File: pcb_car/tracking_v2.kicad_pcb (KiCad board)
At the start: 2 copper layers, 75 x 64 mm, 24 parts, among them J1 Conn_01x02, J2 Conn_01x02, J3 Conn_01x02, J4 Conn_01x02, J5 Conn_01x16_Female, J6 Conn_01x02, J7 Conn_01x20_Female, J8 Conn_01x03, J9 Conn_01x03, SW1 SW_Push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

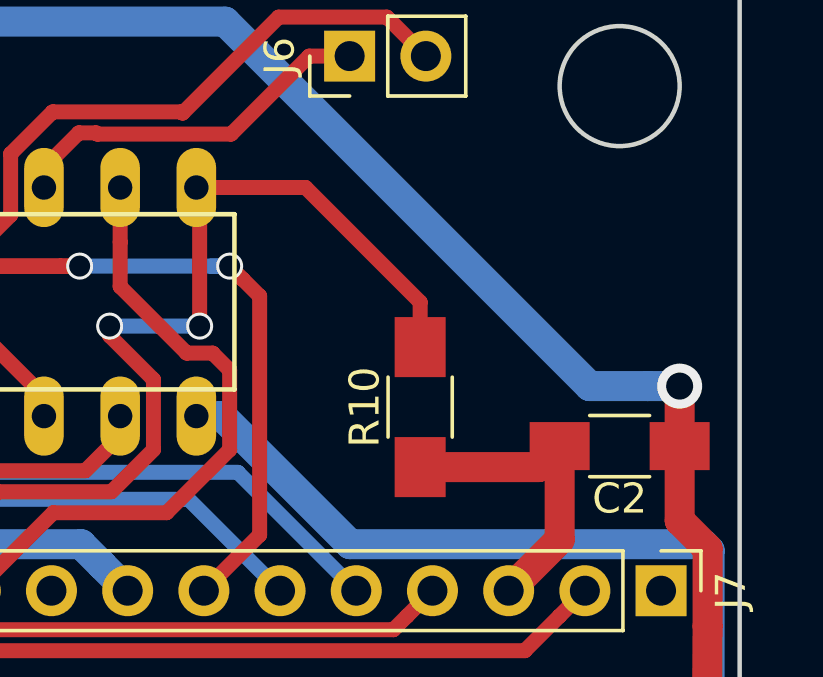
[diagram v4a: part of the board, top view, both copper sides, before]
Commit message: modifications for silkscreen
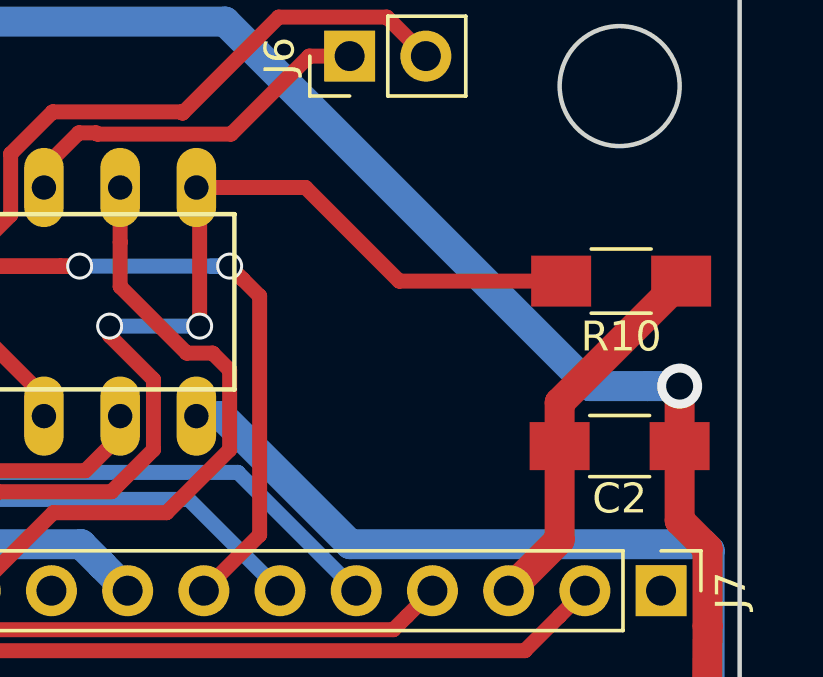
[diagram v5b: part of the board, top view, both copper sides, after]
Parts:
- moved R10 7.91 mm to (190.1, 84.5), turned to 180 degrees
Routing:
- net EN2_B: track 34.0 -> 36.9 mm
- net GND: track 207.0 -> 209.4 mm
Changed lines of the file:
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@@
 (kicad_pcb (version 4) (host pcbnew 4.0.7)
   (general
-    (links 71)
-    (no_connects 3)
-    (area 118.924999 73.924999 194.075001 138.075001)
+    (links 69)
+    (no_connects 0)
+    (area 109.899999 61.3 214.85 145.100001)
     (thickness 1.6)
     (drawings 36)
@@
       (outputformat 1)
       (mirror false)
-      (drillshape 1)
+      (drillshape 0)
       (scaleselection 1)
-      (outputdirectory ""))
+      (outputdirectory ../../../../Desktop/))
   )
   (net 0 "")
@@
   )
   (module Resistors_SMD:R_1206_HandSoldering (layer F.Cu)
-    (at 183.35 88.7 90)
+    (at 190.05 84.5 180)
     (descr "Resistor SMD 1206, hand soldering")
     (tags "resistor 1206")
     (attr smd)
-    (fp_text reference R10 (at 0 -1.85 90) (layer F.SilkS)
-      (effects (font (size 1 1) (thickness 0.15)))
-    )
-    (fp_text value R (at 0 1.9 90) (layer F.Fab)
-      (effects (font (size 1 1) (thickness 0.15)))
-    )
-    (fp_text user %R (at 0 -0.3 90) (layer F.Fab)
+    (fp_text reference R10 (at 0 -1.85 180) (layer F.SilkS)
+      (effects (font (size 1 1) (thickness 0.15)))
+    )
+    (fp_text value R (at 0 1.9 180) (layer F.Fab)
+      (effects (font (size 1 1) (thickness 0.15)))
+    )
+    (fp_text user %R (at -0.25 -0.2 180) (layer F.Fab)
       (effects (font (size 0.7 0.7) (thickness 0.105)))
     )
@@
     (fp_line (start 3.25 1.1) (end 3.25 -1.11) (layer F.CrtYd) (width 0.05))
     (fp_line (start 3.25 1.1) (end -3.25 1.1) (layer F.CrtYd) (width 0.05))
-    (pad 1 smd rect (at -2 0 90) (size 2 1.7) (layers F.Cu F.Paste F.Mask)
-      (net 5 GND))
-    (pad 2 smd rect (at 2 0 90) (size 2 1.7) (layers F.Cu F.Paste F.Mask)
+    (pad 1 smd rect (at -2 0 180) (size 2 1.7) (layers F.Cu F.Paste F.Mask)
+      (net 5 GND))
+    (pad 2 smd rect (at 2 0 180) (size 2 1.7) (layers F.Cu F.Paste F.Mask)
       (net 24 EN2_B))
     (model ${KISYS3DMOD}/Resistors_SMD.3dshapes/R_1206.wrl
@@
   (via (at 154 120) (size 0.9) (drill 0.7) (layers F.Cu B.Cu) (net 4))
   (segment (start 156 117.96) (end 155.77 117.73) (width 0.5) (layer F.Cu) (net 4))
+  (segment (start 188 90) (end 188 88.55) (width 1) (layer F.Cu) (net 5))
+  (segment (start 188 88.55) (end 192.05 84.5) (width 1) (layer F.Cu) (net 5))
+  (segment (start 191.9 84.5) (end 192.05 84.5) (width 1) (layer F.Cu) (net 5))
   (segment (start 183.65 122.95) (end 187.05 122.95) (width 1) (layer F.Cu) (net 5))
   (segment (start 187.05 122.95) (end 188 122) (width 1) (layer F.Cu) (net 5))
@@
   (segment (start 181.17 118.932081) (end 182.8 120.562081) (width 1) (layer B.Cu) (net 5))
   (segment (start 182.8 120.562081) (end 185.437919 120.562081) (width 1) (layer B.Cu) (net 5))
-  (segment (start 183.35 90.7) (end 187.3 90.7) (width 1) (layer F.Cu) (net 5))
-  (segment (start 187.3 90.7) (end 188 90) (width 1) (layer F.Cu) (net 5))
   (segment (start 188 90) (end 188 93.12) (width 1) (layer F.Cu) (net 5))
   (segment (start 188 93.12) (end 186.3 94.82) (width 1) (layer F.Cu) (net 5))
@@
   (segment (start 173.35 83.2008) (end 173.35 81.38) (width 0.5) (layer F.Cu) (net 23))
   (segment (start 173.35 81.38) (end 173.35 81.65) (width 0.5) (layer F.Cu) (net 23))
-  (segment (start 183.35 86.7) (end 183.35 85.2) (width 0.5) (layer F.Cu) (net 24))
-  (segment (start 183.35 85.2) (end 179.53 81.38) (width 0.5) (layer F.Cu) (net 24))
-  (segment (start 179.53 81.38) (end 177.0504 81.38) (width 0.5) (layer F.Cu) (net 24))
-  (segment (start 177.0504 81.38) (end 175.89 81.38) (width 0.5) (layer F.Cu) (net 24))
+  (segment (start 175.89 81.38) (end 179.53 81.38) (width 0.5) (layer F.Cu) (net 24))
+  (segment (start 182.65 84.5) (end 188.05 84.5) (width 0.5) (layer F.Cu) (net 24))
+  (segment (start 179.53 81.38) (end 182.65 84.5) (width 0.5) (layer F.Cu) (net 24))
   (segment (start 176 85.999992) (end 176 81.49) (width 0.5) (layer F.Cu) (net 24))
   (segment (start 176 81.49) (end 175.89 81.38) (width 0.5) (layer F.Cu) (net 24))

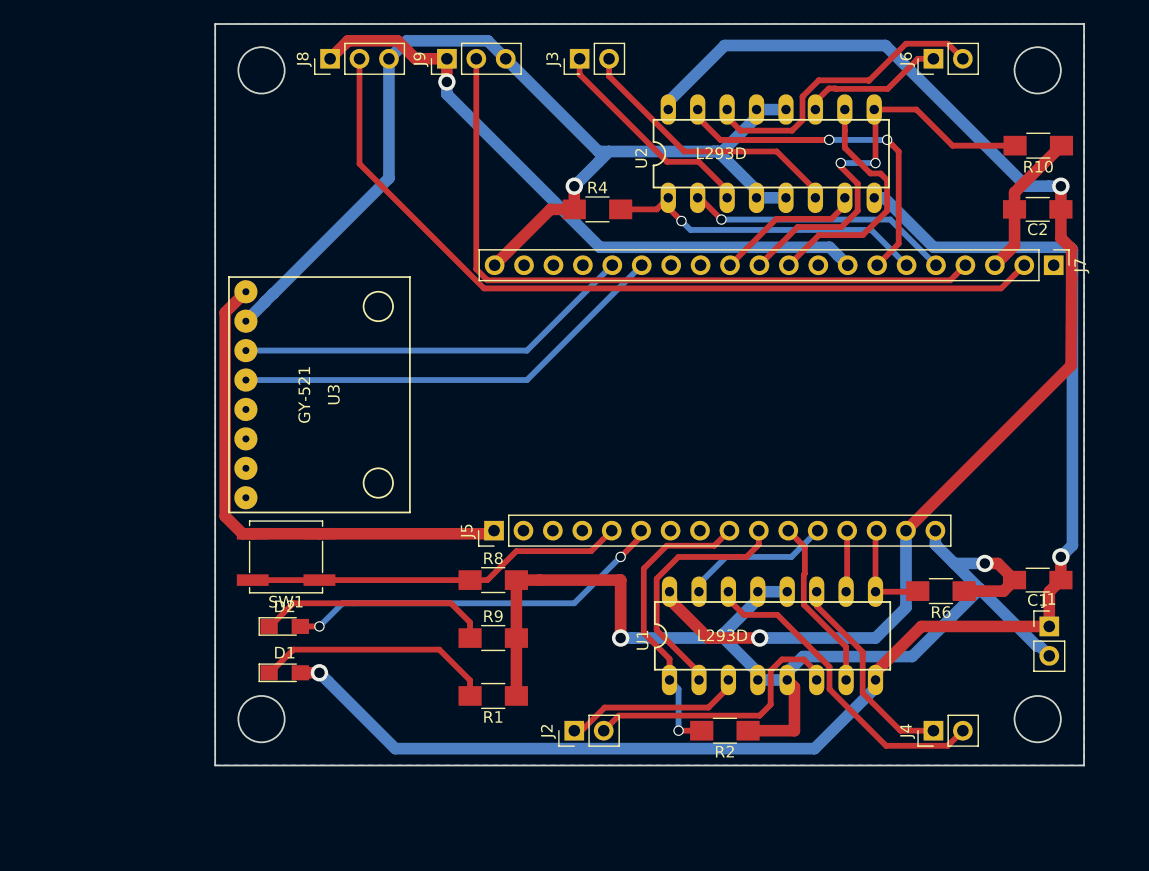
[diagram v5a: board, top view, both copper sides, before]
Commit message: Minor routing change to the Back layer
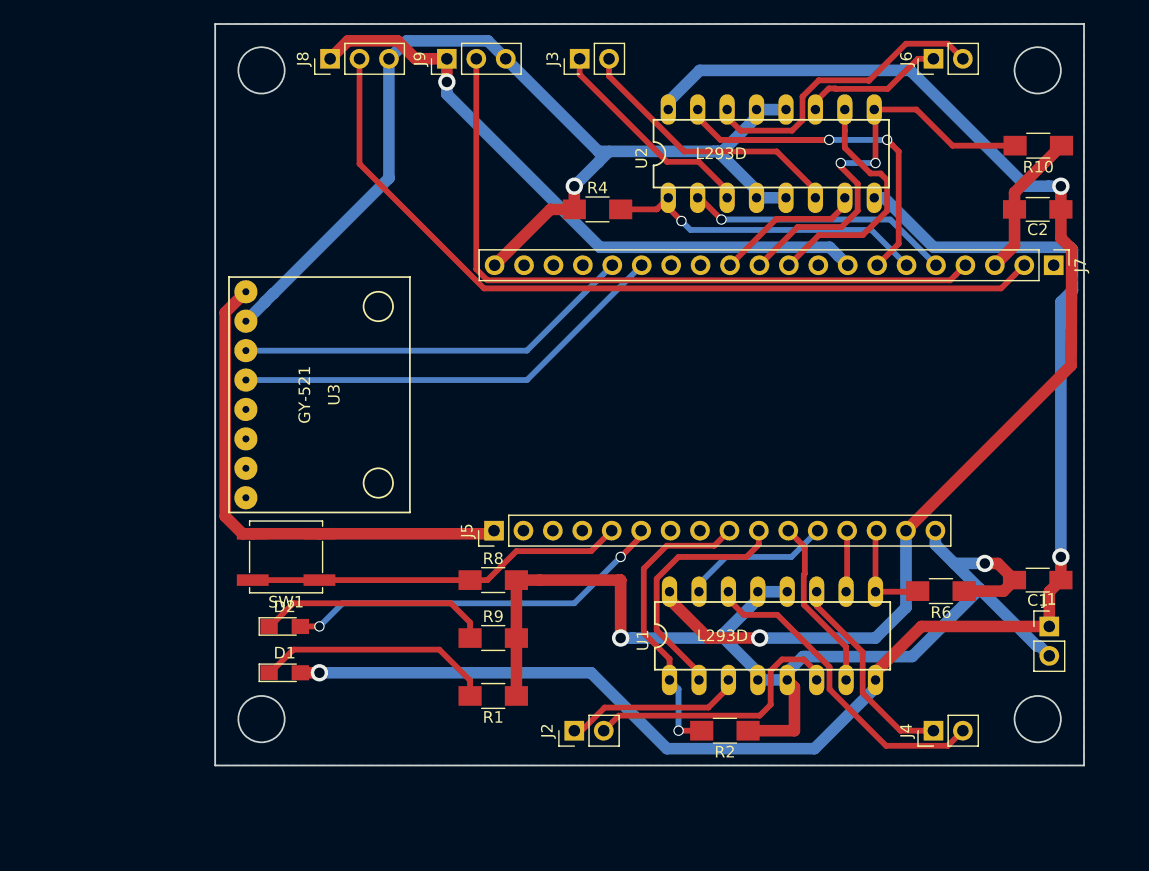
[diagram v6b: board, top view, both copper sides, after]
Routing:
- net 5V: track 107.8 -> 106.1 mm
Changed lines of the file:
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@@
     (links 69)
     (no_connects 0)
-    (area 109.899999 61.3 214.85 145.100001)
+    (area 118.924999 73.924999 194.075001 138.075001)
     (thickness 1.6)
     (drawings 36)
-    (tracks 324)
+    (tracks 325)
     (zones 0)
     (modules 24)
@@
     (40 Dwgs.User user)
     (41 Cmts.User user)
-    (42 Eco1.User user hide)
+    (42 Eco1.User user)
     (43 Eco2.User user)
     (44 Edge.Cuts user)
@@
   (segment (start 123.75 130) (end 125.75 128) (width 0.5) (layer F.Cu) (net 1))
   (segment (start 141 132) (end 141 130.65) (width 0.5) (layer F.Cu) (net 1))
-  (segment (start 128.749999 130.749999) (end 128 130) (width 1) (layer B.Cu) (net 2))
-  (segment (start 134.550001 136.550001) (end 128.749999 130.749999) (width 1) (layer B.Cu) (net 2))
-  (segment (start 170.730399 136.550001) (end 134.550001 136.550001) (width 1) (layer B.Cu) (net 2))
+  (segment (start 193 93.479998) (end 193 97) (width 1) (layer B.Cu) (net 2))
+  (segment (start 192 120) (end 192 98) (width 1) (layer B.Cu) (net 2))
+  (segment (start 192 98) (end 193 97) (width 1) (layer B.Cu) (net 2))
+  (segment (start 170.730399 136.550001) (end 158 136.550001) (width 1) (layer B.Cu) (net 2))
+  (segment (start 128 130) (end 151.449999 130) (width 1) (layer B.Cu) (net 2))
+  (segment (start 151.449999 130) (end 158 136.550001) (width 1) (layer B.Cu) (net 2))
   (segment (start 176 131.2804) (end 170.730399 136.550001) (width 1) (layer B.Cu) (net 2))
   (segment (start 176 130.62) (end 176 131.2804) (width 1) (layer B.Cu) (net 2))
@@
   (via (at 128 130) (size 1.5) (drill 0.9) (layers F.Cu B.Cu) (net 2))
   (segment (start 192 120) (end 192 122) (width 1) (layer F.Cu) (net 2))
-  (segment (start 193 93.479998) (end 193 119) (width 1) (layer B.Cu) (net 2))
   (via (at 192 120) (size 1.5) (drill 0.9) (layers F.Cu B.Cu) (net 2))
-  (segment (start 193 119) (end 192 120) (width 1) (layer B.Cu) (net 2))
   (segment (start 175.89 89) (end 176.743516 89) (width 1) (layer B.Cu) (net 2))
   (segment (start 176.743516 89) (end 181.013515 93.269999) (width 1) (layer B.Cu) (net 2))
@@
   (segment (start 168.38 123) (end 165.84 123) (width 1) (layer B.Cu) (net 5))
   (segment (start 168.38 122.3396) (end 168.38 123) (width 1) (layer B.Cu) (net 5))
+  (segment (start 179 78) (end 189 88) (width 1) (layer B.Cu) (net 6))
   (segment (start 158.11 81.38) (end 158.11 80.7196) (width 1) (layer B.Cu) (net 6))
-  (segment (start 158.11 80.7196) (end 162.979645 75.849955) (width 1) (layer B.Cu) (net 6))
-  (segment (start 162.979645 75.849955) (end 176.849955 75.849955) (width 1) (layer B.Cu) (net 6))
-  (segment (start 176.849955 75.849955) (end 189 88) (width 1) (layer B.Cu) (net 6))
+  (segment (start 158.11 80.7196) (end 160.8296 78) (width 1) (layer B.Cu) (net 6))
+  (segment (start 160.8296 78) (end 179 78) (width 1) (layer B.Cu) (net 6))
   (segment (start 189 88) (end 190.93934 88) (width 1) (layer B.Cu) (net 6))
   (segment (start 190.93934 88) (end 192 88) (width 1) (layer B.Cu) (net 6))

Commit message: Removed unnecessary vias and tracks
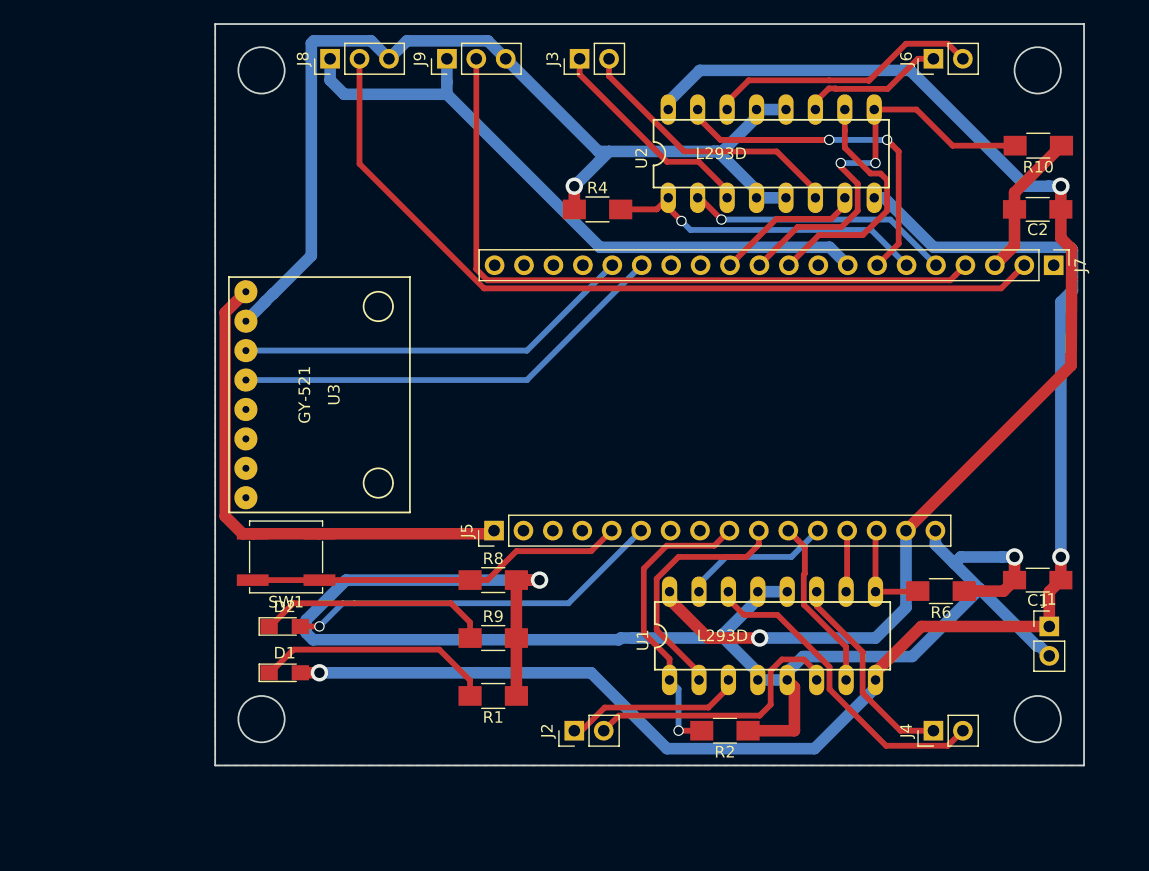
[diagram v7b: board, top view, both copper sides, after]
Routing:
- net GND: track 209.4 -> 246.2 mm
- net Net-(J6-Pad2): track 27.0 -> 24.3 mm
- net 3V3: track 55.1 -> 56.2 mm, vias 1 -> 0
- net Net-(D2-Pad2): track 33.5 -> 33.7 mm, vias 2 -> 1

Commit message: final version
added silkscreen
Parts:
- added G***: LOGO, Desktop:LOGO, F.Cu at (157.3, 106.1)
- moved R10 9.10 mm to (182.8, 90.0)
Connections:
- J7 pad 12: IN2_B -> EN1_B
- J7 pad 6: EN1_B -> IN2_B
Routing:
- net EN1_B: track 28.7 -> 12.7 mm, vias 1 -> 0
- net GND: track 246.2 -> 242.0 mm
- net EN2_B: track 36.9 -> 33.6 mm
- net IN2_B: track 13.4 -> 10.0 mm, vias 0 -> 1
